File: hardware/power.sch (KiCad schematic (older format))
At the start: 39 parts, among them Q1 Si3129DV, Q3 Si1967DH, U1 MAX17521, U2 AP2139AK-3.3

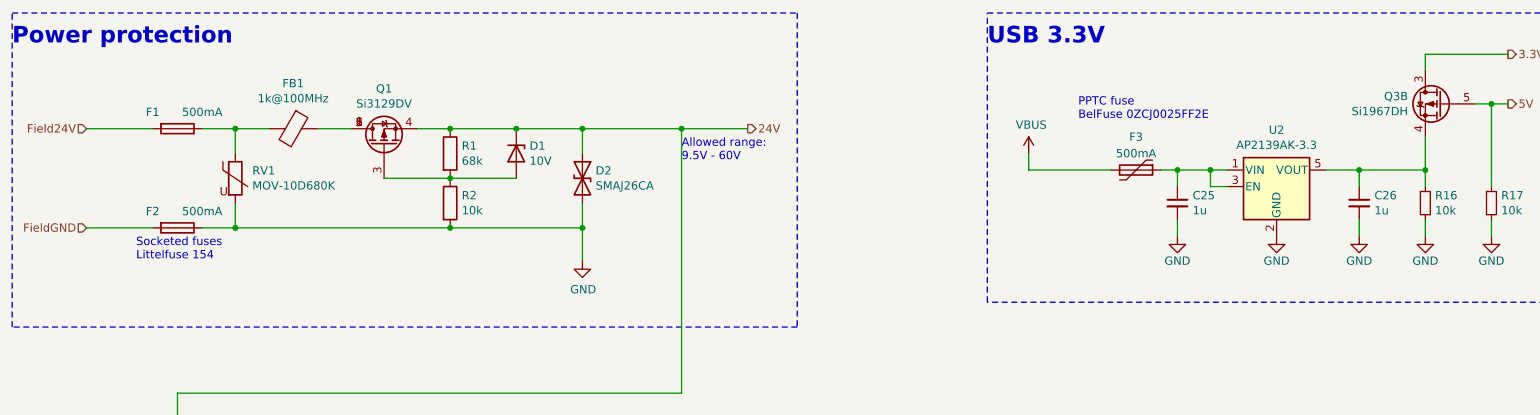
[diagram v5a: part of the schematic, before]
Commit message: Power routing
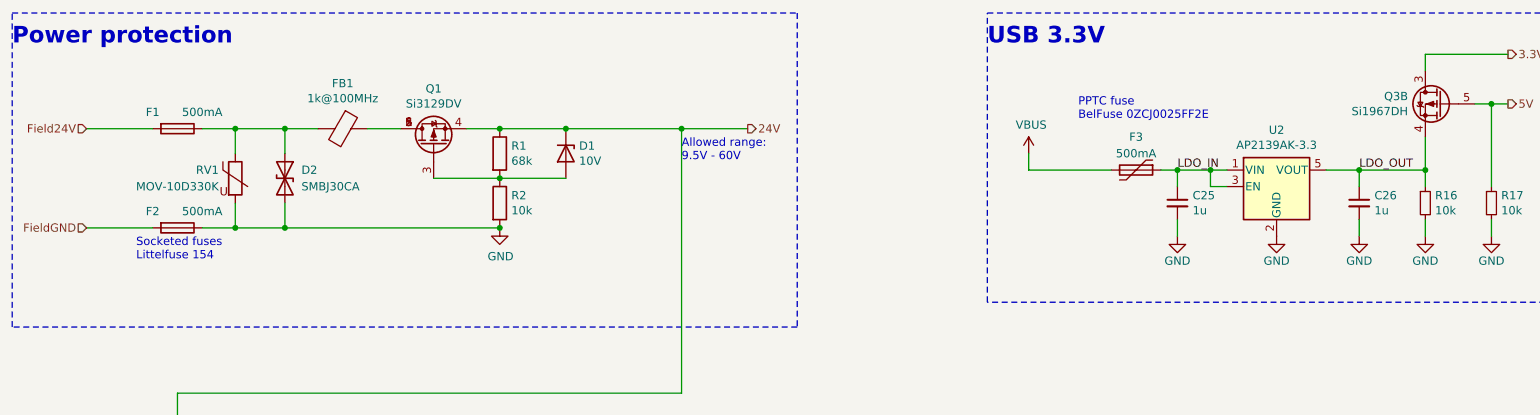
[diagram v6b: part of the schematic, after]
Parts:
- D1: footprint Diode_SMD:D_MiniMELF -> Diode_SMD:D_SOD-323F
- D2: value SMAJ26CA -> SMBJ30CA; footprint Diode_SMD:D_SMA -> Diode_SMD:D_SMB
- RV1: value MOV-10D680K -> MOV-10D330K
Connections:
- net 24V: no longer D2.1 (A1)
- net LDO_IN: now reaches C25.1, F3.1, U2.1 (VIN), U2.3 (EN)
- net at F1.1, FB1.2, RV1.1: now also D2.1 (A1)
- net LDO_OUT: now reaches C26.1, Q3.4 (S), R16.1, U2.5 (VOUT)
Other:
- moved on the sheet: D1, D2, FB1, Q1, R1, R2
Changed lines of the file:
@@
 L Device:R R2
 U 1 1 6128C2CE
-P 3350 1800
-F 0 "R2" H 3420 1846 50  0000 L CNN
-F 1 "10k" H 3420 1755 50  0000 L CNN
-F 2 "Resistor_SMD:R_0805_2012Metric" V 3280 1800 50  0001 C CNN
-F 3 "~" H 3350 1800 50  0001 C CNN
-	1    3350 1800
+P 3650 1800
+F 0 "R2" H 3720 1846 50  0000 L CNN
+F 1 "10k" H 3720 1755 50  0000 L CNN
+F 2 "Resistor_SMD:R_0805_2012Metric" V 3580 1800 50  0001 C CNN
+F 3 "~" H 3650 1800 50  0001 C CNN
+	1    3650 1800
 	1    0    0    -1
 $EndComp
@@
 L Device:D_Zener D1
 U 1 1 6128CDAA
-P 3750 1500
-F 0 "D1" V 3704 1580 50  0000 L CNN
-F 1 "10V" V 3795 1580 50  0000 L CNN
-F 2 "Diode_SMD:D_MiniMELF" H 3750 1500 50  0001 C CNN
-F 3 "https://hu.mouser.com/ProductDetail/Rectron/ZMM5240B?qs=SBE%252BrxyZI43k0KP276ZIqw%3D%3D" H 3750 1500 50  0001 C CNN
-	1    3750 1500
-	0    1    1    0
-$EndComp
-Wire Wire Line
-	2950 1650 3350 1650
-Connection ~ 3350 1650
+P 4050 1500
+F 0 "D1" V 4004 1580 50  0000 L CNN
+F 1 "10V" V 4095 1580 50  0000 L CNN
+F 2 "Diode_SMD:D_SOD-323F" H 4050 1500 50  0001 C CNN
+F 3 "https://hu.mouser.com/ProductDetail/Diodes-Incorporated/DDZ10CSF-7?qs=gfe7vQ8txpVWWxdcO1kGxQ%3D%3D" H 4050 1500 50  0001 C CNN
+	1    4050 1500
+	0    1    1    0
+$EndComp
+Wire Wire Line
+	3250 1650 3650 1650
+Connection ~ 3650 1650
 Wire Wire Line
 	1850 1950 2050 1950
@@
 	2050 1950 2050 1800
 Wire Wire Line
-	3350 1350 3150 1350
-Wire Wire Line
-	2250 1350 2050 1350
+	3650 1350 3450 1350
 Wire Wire Line
 	2050 1350 2050 1500
@@
 L Device:D_TVS D2
 U 1 1 612A1A78
-P 4150 1650
-F 0 "D2" V 4104 1730 50  0000 L CNN
-F 1 "SMAJ26CA" V 4195 1730 50  0000 L CNN
-F 2 "Diode_SMD:D_SMA" H 4150 1650 50  0001 C CNN
-F 3 "~" H 4150 1650 50  0001 C CNN
-	1    4150 1650
+P 2350 1650
+F 0 "D2" V 2300 1750 50  0000 L CNN
+F 1 "SMBJ30CA" V 2400 1750 50  0000 L CNN
+F 2 "Diode_SMD:D_SMB" H 2350 1650 50  0001 C CNN
+F 3 "~" H 2350 1650 50  0001 C CNN
+	1    2350 1650
 	0    1    1    0
 $EndComp
@@
 L Device:Ferrite_Bead FB1
 U 1 1 612A82A6
-P 2400 1350
-F 0 "FB1" V 2126 1350 50  0000 C CNN
-F 1 "1k@100MHz" V 2217 1350 50  0000 C CNN
-F 2 "Inductor_SMD:L_0805_2012Metric" V 2330 1350 50  0001 C CNN
-F 3 "~" H 2400 1350 50  0001 C CNN
-	1    2400 1350
-	0    1    1    0
-$EndComp
-Wire Wire Line
-	2550 1350 2750 1350
-Wire Wire Line
-	2050 1950 3350 1950
-Connection ~ 2050 1950
-Connection ~ 3350 1350
+P 2700 1350
+F 0 "FB1" V 2426 1350 50  0000 C CNN
+F 1 "1k@100MHz" V 2517 1350 50  0000 C CNN
+F 2 "Inductor_SMD:L_0805_2012Metric" V 2630 1350 50  0001 C CNN
+F 3 "~" H 2700 1350 50  0001 C CNN
+	1    2700 1350
+	0    1    1    0
+$EndComp
+Wire Wire Line
+	2850 1350 3050 1350
+Wire Wire Line
+	2350 1950 3650 1950
+Connection ~ 3650 1350
 $Comp
 L power:GND #PWR05
 U 1 1 612B5B37
-P 4150 2150
-F 0 "#PWR05" H 4150 1900 50  0001 C CNN
-F 1 "GND" H 4155 1977 50  0000 C CNN
-F 2 "" H 4150 2150 50  0001 C CNN
-F 3 "" H 4150 2150 50  0001 C CNN
-	1    4150 2150
-	1    0    0    -1
-$EndComp
-Connection ~ 3350 1950
+P 3650 1950
+F 0 "#PWR05" H 3650 1700 50  0001 C CNN
+F 1 "GND" H 3655 1777 50  0000 C CNN
+F 2 "" H 3650 1950 50  0001 C CNN
+F 3 "" H 3650 1950 50  0001 C CNN
+	1    3650 1950
+	1    0    0    -1
+$EndComp
 $Comp
 L Device:R R1
 U 1 1 612D74A8
-P 3350 1500
-F 0 "R1" H 3420 1546 50  0000 L CNN
-F 1 "68k" H 3420 1455 50  0000 L CNN
-F 2 "Resistor_SMD:R_0805_2012Metric" V 3280 1500 50  0001 C CNN
-F 3 "~" H 3350 1500 50  0001 C CNN
-	1    3350 1500
-	1    0    0    -1
-$EndComp
-Connection ~ 3750 1350
-Wire Wire Line
-	3750 1650 3350 1650
-Wire Wire Line
-	3350 1350 3750 1350
-Wire Wire Line
-	4150 1350 4150 1500
-Wire Wire Line
-	3750 1350 4150 1350
-Wire Wire Line
-	4150 1800 4150 1950
-Wire Wire Line
-	4150 1950 3350 1950
-Wire Wire Line
-	4150 2150 4150 1950
-Connection ~ 4150 1950
-Connection ~ 4150 1350
+P 3650 1500
+F 0 "R1" H 3720 1546 50  0000 L CNN
+F 1 "68k" H 3720 1455 50  0000 L CNN
+F 2 "Resistor_SMD:R_0805_2012Metric" V 3580 1500 50  0001 C CNN
+F 3 "~" H 3650 1500 50  0001 C CNN
+	1    3650 1500
+	1    0    0    -1
+$EndComp
+Wire Wire Line
+	4050 1650 3650 1650
+Wire Wire Line
+	3650 1350 4050 1350
 $Comp
 L Si3129DV:Si3129DV Q1
 U 1 1 612EDE3D
-P 2950 1450
-F 0 "Q1" V 3292 1450 50  0000 C CNN
-F 1 "Si3129DV" V 3201 1450 50  0000 C CNN
-F 2 "Package_SO:TSOP-6_1.65x3.05mm_P0.95mm" H 3150 1550 50  0001 C CNN
-F 3 "https://www.vishay.com/docs/78984/si3129dv.pdf" H 2950 1450 50  0001 C CNN
-	1    2950 1450
+P 3250 1450
+F 0 "Q1" V 3592 1450 50  0000 C CNN
+F 1 "Si3129DV" V 3501 1450 50  0000 C CNN
+F 2 "Package_SO:TSOP-6_1.65x3.05mm_P0.95mm" H 3450 1550 50  0001 C CNN
+F 3 "https://www.vishay.com/docs/78984/si3129dv.pdf" H 3250 1450 50  0001 C CNN
+	1    3250 1450
 	0    -1   -1   0
 $EndComp
@@
 U 1 1 612F133A
 P 2050 1650
-F 0 "RV1" H 2153 1696 50  0000 L CNN
-F 1 "MOV-10D680K" H 2153 1605 50  0000 L CNN
+F 0 "RV1" H 1950 1700 50  0000 R CNN
+F 1 "MOV-10D330K" H 1950 1600 50  0000 R CNN
 F 2 "Varistor:RV_Disc_D12mm_W4.4mm_P7.5mm" V 1980 1650 50  0001 C CNN
 F 3 "~" H 2050 1650 50  0001 C CNN
@@
 Wire Notes Line
 	700  2550 700  650
-Wire Wire Line
-	4150 1350 4750 1350
 Wire Notes Line
 	700  3350 6150 3350
@@
 Wire Wire Line
 	1700 2950 1700 3950
-Connection ~ 4750 1350
 Wire Wire Line
 	4750 1350 5150 1350
@@
 Text Label 3000 4750 2    50   ~ 0
 MODE2
+Text Label 7750 1600 0    50   ~ 0
+LDO_IN
+Text Label 8850 1600 0    50   ~ 0
+LDO_OUT
+Connection ~ 3650 1950
+Wire Wire Line
+	2350 1350 2350 1500
+Wire Wire Line
+	2050 1350 2350 1350
+Wire Wire Line
+	2350 1800 2350 1950
+Wire Wire Line
+	2350 1950 2050 1950
+Connection ~ 2050 1950
+Wire Wire Line
+	2550 1350 2350 1350
+Connection ~ 2350 1350
+Connection ~ 2350 1950
+Wire Wire Line
+	4050 1350 4750 1350
+Connection ~ 4050 1350
+Connection ~ 4750 1350
 $EndSCHEMATC
